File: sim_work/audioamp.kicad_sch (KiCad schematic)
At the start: 28 parts, among them Q1 2N3904, Q2 2N3904, Q3 2N3906, Q4 2N3904, Q5 2N3904, Q6 2N3906, Q7 2N2219A, Q8 2N2219A

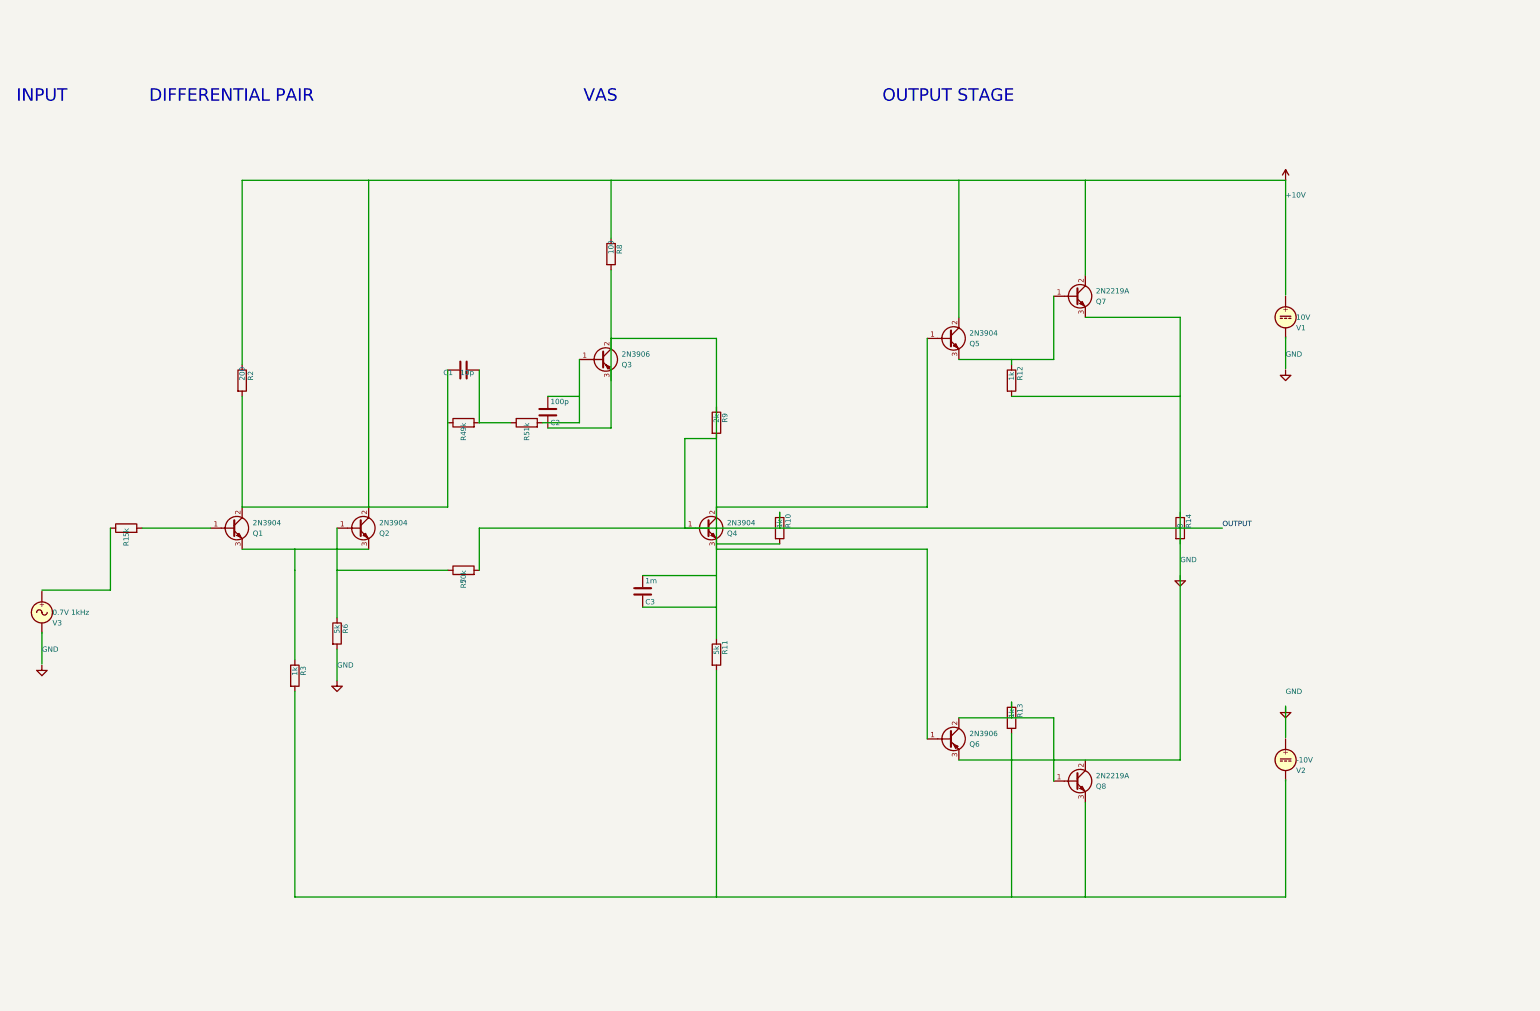
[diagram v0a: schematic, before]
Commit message: Zero wire crossings: audioamp schematic clean routing
Eliminated all wire crossings (was 5-7, now 0) by:
- R7 feedback via net labels instead of long physical wires
- C3 bootstrap routed to Q3C (same VAS net) avoiding R9/Q4B vertical
- Q6C->Q8B chained through R13, Q4E->Q6B via R11 pin1
- R12 VH routing, C3 VH routing to separate vertical columns
Wire crossings now enforced as ERROR (was WARNING).

Co-Authored-By: Claude Opus 4.6 <noreply@anthropic.com>
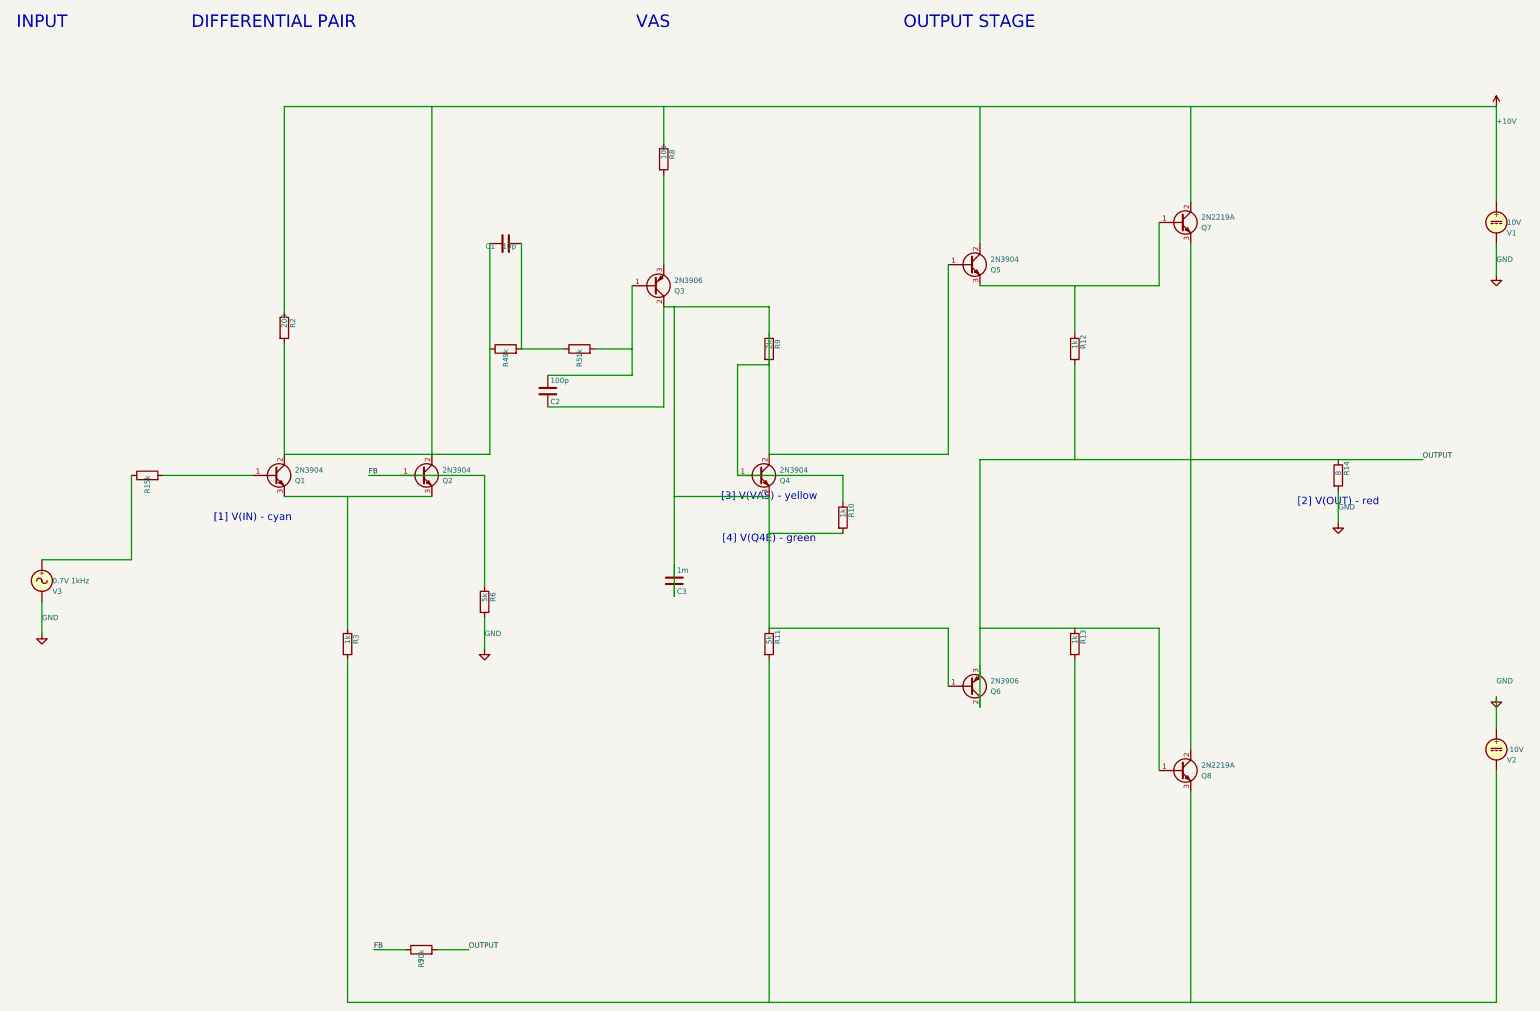
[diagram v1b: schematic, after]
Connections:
- net +10V: now also V1.1
- net GND: now also R14.2, V1.2, V2.1, V3.2
- net OUTPUT: now also Q6.2 (C), R14.1; no longer Q6.3 (E), Q7.3 (E)
- net at Q8.1 (B): now also R13.1; no longer Q6.2 (C)
- net at Q8.2 (C): now also Q7.3 (E)
- net at Q4.3 (E), Q6.1 (B): now also R11.1
- net at Q4.1 (B), R9.2: now also R10.1
- net at Q3.2 (C), Q4.2 (C), Q5.1 (B): now also C2.2; no longer R11.1
- net at R1.1: now also V3.1
- net at V2.2: now also R3.2
- net FB: now reaches Q2.1 (B), R6.1
- net FB: now also R7.1
- net at C2.1: now also Q3.1 (B)
- net at R8.2: now also Q3.3 (E); no longer C2.2
- net at R5.2: no longer Q3.1 (B)
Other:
- note added: "[1] V(IN) - cyan"
- note added: "[2] V(OUT) - red"
- note added: "[3] V(VAS) - yellow"
- note added: "[4] V(Q4E) - green"
